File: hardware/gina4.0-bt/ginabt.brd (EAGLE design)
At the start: 25 x 15 mm, 27 parts, among them U1 CC2541, U2 MPU-9150, U3 CCDEBUGGER, U5 TPS71530

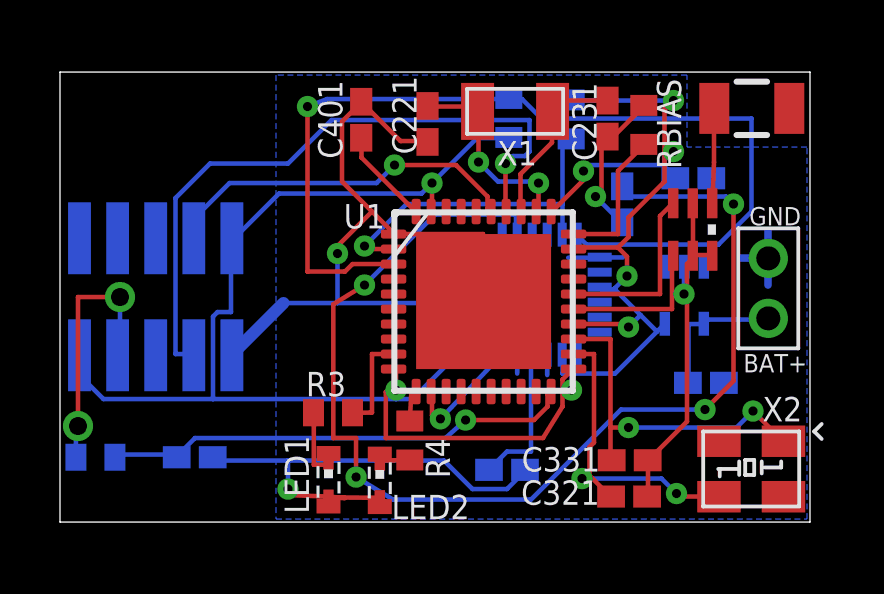
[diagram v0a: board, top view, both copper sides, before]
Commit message: resolving bugs in the layout. adding bom
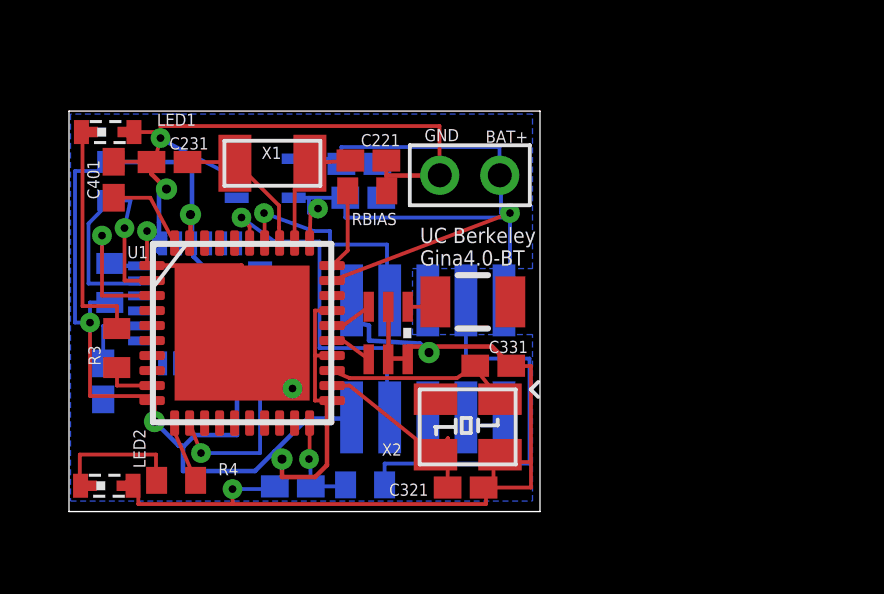
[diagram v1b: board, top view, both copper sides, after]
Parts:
- moved C3 18.3 mm to (1.44, 4.69)
- moved R1 15.5 mm to (1.69, 11.4)
- moved C231 14.7 mm to (3.65, 12.0), turned to 180 degrees
- moved U5 14.5 mm to (6.84, 11.5), turned to 90 degrees
- moved R2 14.4 mm to (1.66, 7.97)
- moved LED1 13.7 mm to (1.59, 13.0), turned to 270 degrees
- moved C5 13.7 mm to (9.98, 11.9)
- moved U2 11.3 mm to (4.67, 7.29), turned to 270 degrees
- moved U$4 11.3 mm to (13.8, 7.34)
- moved C4 11.0 mm to (10.1, 10.8)
- moved F1 10.7 mm to (10.9, 6.30)
- moved X2 9.55 mm to (13.6, 3.17)
- moved RBIAS 9.48 mm to (10.2, 11.0), turned to 180 degrees
- moved U3 9.30 mm to (12.3, 5.44), turned to 180 degrees
- moved LED2 9.10 mm to (1.56, 1.21), turned to 270 degrees
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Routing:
- net N$14: track 38.8 -> 2.48 mm, vias 4 -> 0
- net SDA: track 33.1 -> 7.04 mm
- net DC: track 22.4 -> 7.63 mm
- net N$20: track 15.8 -> 3.38 mm
- net GND: track 60.3 -> 71.0 mm, vias 4 -> 6
- net N$15: track 2.27 -> 8.23 mm
- net +3V3: track 73.8 -> 67.9 mm, vias 8 -> 6
- net N$7: track 11.7 -> 6.35 mm, vias 2 -> 0
- net N$8: track 6.09 -> 1.43 mm
- net N$6: track 11.0 -> 6.59 mm, vias 2 -> 0
- net N$19: track 8.78 -> 13.1 mm, vias 2 -> 0
- net N$10: track 4.91 -> 1.14 mm
- net N$2: track 1.11 -> 4.86 mm
- net +18V: track 4.72 -> 8.40 mm
- net N$9: track 5.08 -> 1.43 mm
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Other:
- board size 25 x 15 mm -> 15.7 x 13.3 mm
- board text added: "Gina4.0-BT"
- board text added: "UC Berkeley"
- board text removed: "Gina4.0-bt UC Berkeley"
